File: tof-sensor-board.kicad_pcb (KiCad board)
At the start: 2 copper layers, 39 parts, among them IC1 TLV710, U1 STM32F042C6T6, U2 LTC2875, U3 VL6180X, X1 16MHz

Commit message: PCB
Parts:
- added _M2: VAL**, _mech:_M2, F.Cu at (137.1, 102.1)
- added _M2: VAL**, _mech:_M2, F.Cu at (137.1, 79.6)
- C1, C10, C11, C12, C13, C14, C15, C16, C2, C3, C4, C5, C6, C7, C8, C9, D1, D2, D3, D4, F1, IC1, R1, R10, R2, R3, R4, R5, R6, R7, R8, R9, U2, X1: moved to B.Cu
- CONN1: footprint _connectors:_Pin2mm_5z -> _connectors:_SoldarPad2mm_5; moved to B.Cu
- U3: footprint _sensors:VL6180X -> _sensors:VL6180X_EdgeMount
- moved C9 74.9 mm to (133.3, 98.1), turned to 270 degrees
- moved C11 72.7 mm to (136.8, 90.4), turned to 90 degrees
- moved C4 71.1 mm to (138.1, 90.4), turned to 90 degrees
- moved D3 67.7 mm to (143.3, 99.4), turned to 180 degrees
- moved C1 67.5 mm to (138.3, 85.7), turned to 180 degrees
- moved C10 67.0 mm to (136.5, 84.0), turned to 270 degrees
- moved C3 65.5 mm to (138.8, 93.1), turned to 180 degrees
- moved C12 65.0 mm to (135.3, 84.0), turned to 270 degrees
- moved C8 64.8 mm to (138.4, 98.0), turned to 90 degrees
- moved D4 64.7 mm to (133.0, 83.4), turned to 180 degrees
- moved R8 64.2 mm to (132.2, 86.9)
- moved C7 62.7 mm to (140.7, 83.8)
- moved C2 59.8 mm to (143.4, 95.5), turned to 180 degrees
- moved D2 59.7 mm to (143.3, 98.0), turned to 180 degrees
- moved C14 58.3 mm to (142.9, 89.4), turned to 90 degrees
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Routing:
- net GND: track 0.00 -> 111.7 mm, vias 0 -> 10
- net VCC: track 0.00 -> 46.7 mm, vias 0 -> 4
- net /2.8V: track 0.00 -> 26.7 mm, vias 0 -> 2
- net /I2C_SDA: track 0.00 -> 24.2 mm, vias 0 -> 1
- net +5V: track 0.00 -> 22.1 mm, vias 0 -> 1
- net /I2C_SCL: track 0.00 -> 21.6 mm, vias 0 -> 1
- net Net-(CONN2-Pad3): track 0.00 -> 21.4 mm, vias 0 -> 3
- net /STM32F0_SWCLK: track 0.00 -> 19.6 mm, vias 0 -> 1
- net /STM32F0_SWDIO: track 0.00 -> 19.5 mm, vias 0 -> 1
- net Net-(CONN2-Pad4): track 0.00 -> 18.7 mm, vias 0 -> 2
- net /GPIO1: track 0.00 -> 15.1 mm, vias 0 -> 1
- net /STM32F0_NRST: track 0.00 -> 13.2 mm, vias 0 -> 2
- net /GPIO0: track 0.00 -> 10.4 mm, vias 0 -> 1
- net Net-(C8-Pad1): track 0.00 -> 8.64 mm, vias 0 -> 1
- net /Error: track 0.00 -> 7.83 mm, vias 0 -> 1
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- added copper zone on F.Cu, net GND
- added copper zone on B.Cu, net VCC
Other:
- board outline added: 17 x 22.5 mm
- net class Default: clearance 0.2 -> 0.1524; trace_width 0.25 -> 0.1524
- net class Inner added: clearance 0.254, trace_width 0.204, via_dia 0.6, via_drill 0.4
- net class Power added: clearance 0.2, trace_width 0.4, via_dia 0.6, via_drill 0.4
- rule trace_clearance: 0.2 -> 0.1524
- rule trace_min: 0.2 -> 0.1524

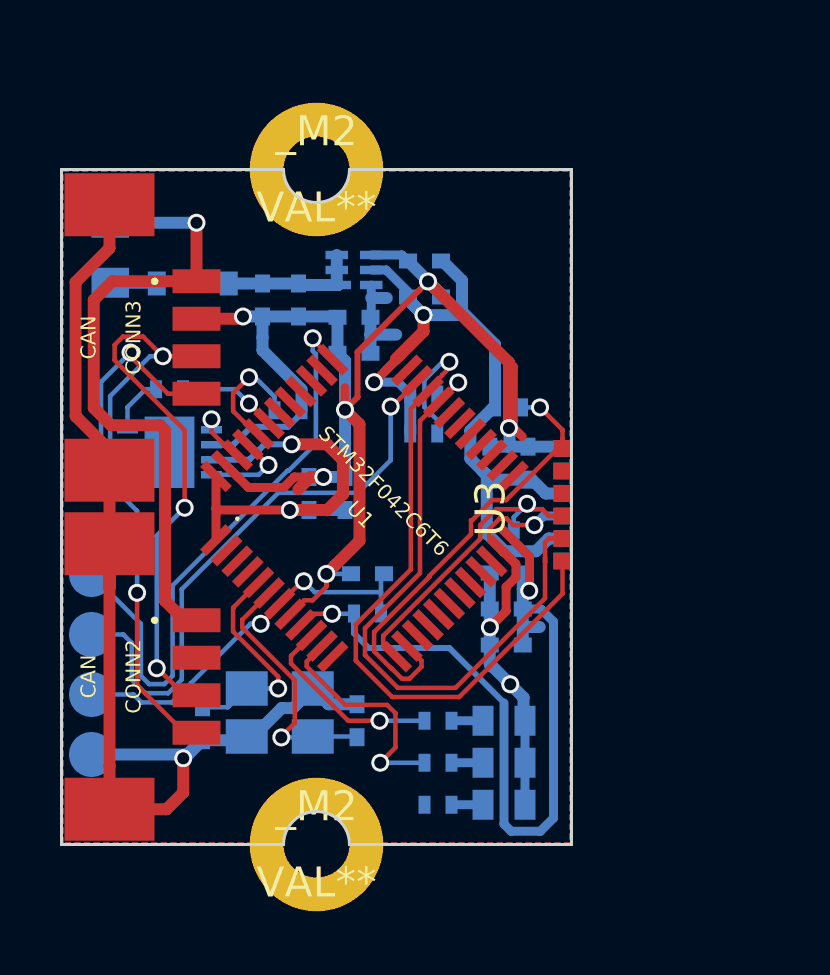
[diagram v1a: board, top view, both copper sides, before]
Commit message: Switch to VL53L0X and QFN32 STM32f302
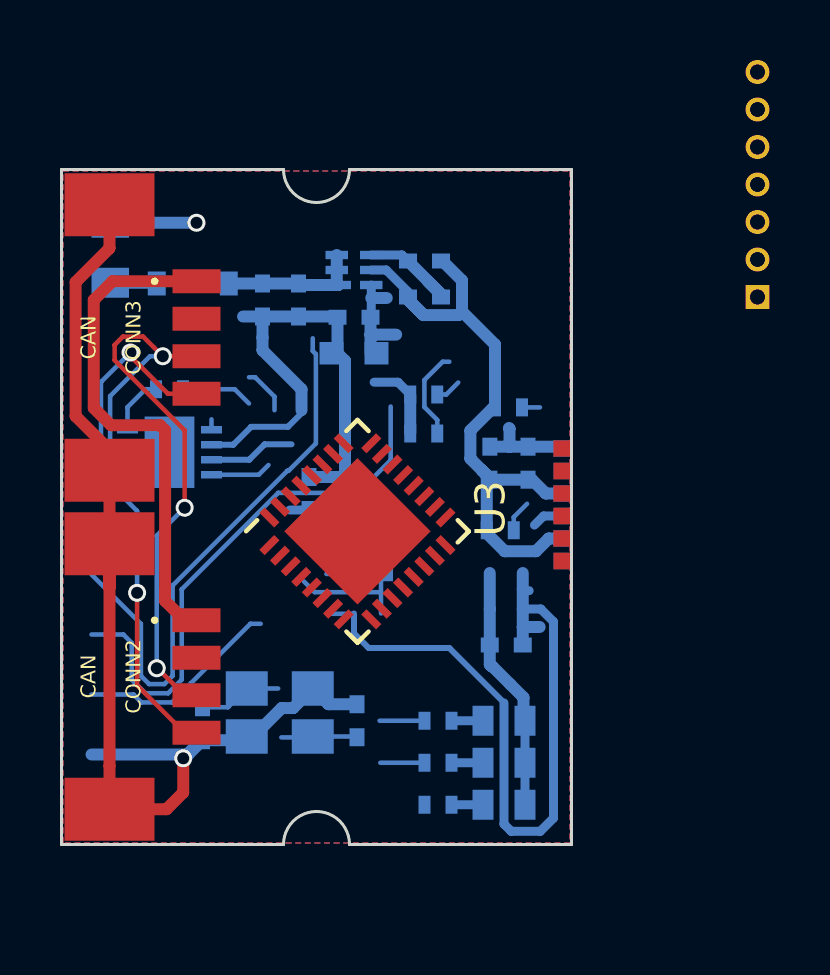
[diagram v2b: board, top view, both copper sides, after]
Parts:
- removed C4: 0.1uF, Capacitors_SMD:C_0402
- removed C5: 1uF, Capacitors_SMD:C_0402
- removed C6: 0.01uF, Capacitors_SMD:C_0402
- removed R1, R2: 100k, Resistors_SMD:R_0402
- removed _M2 (x2): VAL**, _mech:_M2
- C1: footprint Capacitors_SMD:C_0402 -> Capacitors_SMD:C_0603
- CONN1: value SWD -> SWD/DEBUG; footprint _connectors:_SoldarPad2mm_5 -> Connectors_Molex:Connector_Molex_PicoBlade_53048-0710
- U1: value STM32F042C6T6 -> STM32F302K8U6; footprint _lqfp:_LQFP48 -> Housings_DFN_QFN:QFN-32-1EP_5x5mm_Pitch0.5mm
- moved CONN1 25.9 mm to (151.8, 83.8)
- moved U1 4.72 mm to (138.5, 91.7), turned to 45 degrees
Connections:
- C2 pad 1: VCC -> GND
- C2 pad 2: GND -> VCC
- C3 pad 1: /STM32F0_NRST -> (no net)
- C7 pad 1: /2.8V -> VCC
- CONN1 pad 3: /STM32F0_NRST -> /NRST
- CONN1 pad 4: /STM32F0_SWDIO -> /SWDIO
- CONN1 pad 5: /STM32F0_SWCLK -> /SWCLK
- R3 pad 1: /2.8V -> VCC
- R4 pad 1: /2.8V -> VCC
- U1 pad 10: /Proximity -> /GPIO0
- U1 pad 11: /Error -> /GPIO1
- U1 pad 12: Net-(U1-Pad12) -> (no net)
- U1 pad 13: /GPIO0 -> (no net)
- U1 pad 14: /GPIO1 -> (no net)
- U1 pad 15: Net-(U1-Pad15) -> (no net)
- U1 pad 16: Net-(U1-Pad16) -> GND
- U1 pad 17: Net-(U1-Pad17) -> VCC
- U1 pad 18: Net-(U1-Pad18) -> (no net)
- U1 pad 19: Net-(U1-Pad19) -> /I2C_SCL
- U1 pad 2: Net-(U1-Pad2) -> Net-(C9-Pad1)
- U1 pad 20: Net-(U1-Pad20) -> /I2C_SDA
- U1 pad 21: Net-(U1-Pad21) -> /CAN_RX
- U1 pad 22: Net-(U1-Pad22) -> /CAN_TX
- U1 pad 23: GND -> /SWDIO
- U1 pad 24: VCC -> /SWCLK
- U1 pad 25: Net-(U1-Pad25) -> (no net)
- U1 pad 26: Net-(U1-Pad26) -> (no net)
- U1 pad 27: Net-(U1-Pad27) -> (no net)
- U1 pad 28: Net-(U1-Pad28) -> (no net)
- U1 pad 29: Net-(U1-Pad29) -> (no net)
- U1 pad 3: Net-(U1-Pad3) -> Net-(C8-Pad1)
- U1 pad 30: Net-(U1-Pad30) -> (no net)
- U1 pad 31: Net-(U1-Pad31) -> GND
- U1 pad 32: /I2C_SCL -> GND
- U1 pad 33: /I2C_SDA -> (no net)
- U1 pad 4: Net-(U1-Pad4) -> /NRST
- U1 pad 5: Net-(C9-Pad1) -> VCC
- U1 pad 6: Net-(C8-Pad1) -> GND
- U1 pad 7: /STM32F0_NRST -> /Proximity
- U1 pad 8: GND -> /Error
- U1 pad 9: VCC -> /CAN_SPEED
- U2 pad 5: Net-(U2-Pad5) -> (no net)
- U3 pad 11: Net-(U3-Pad11) -> (no net)
- U3 pad 2: Net-(U3-Pad2) -> (no net)
- U3 pad 3: Net-(U3-Pad3) -> (no net)
- U3 pad 7: Net-(U3-Pad7) -> (no net)
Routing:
- net /I2C_SDA: track 24.2 -> 3.04 mm, vias 1 -> 0
- net (no net): track 0.00 -> 21.0 mm
- net /I2C_SCL: track 21.6 -> 0.87 mm, vias 1 -> 0
- net /STM32F0_SWCLK: track 19.6 -> 0.00 mm, vias 1 -> 0
- net /STM32F0_SWDIO: track 19.5 -> 0.00 mm, vias 1 -> 0
- net /SWDIO: track 0.00 -> 18.6 mm
- net GND: track 111.7 -> 93.1 mm, vias 10 -> 1
- net VCC: track 46.7 -> 28.5 mm, vias 4 -> 0
- net /GPIO1: track 15.1 -> 0.60 mm, vias 1 -> 0
- net /STM32F0_NRST: track 13.2 -> 0.00 mm, vias 2 -> 0
- net /GPIO0: track 10.4 -> 1.07 mm, vias 1 -> 0
- net /2.8V: track 26.7 -> 18.3 mm, vias 2 -> 0
- net /Error: track 7.83 -> 1.47 mm, vias 1 -> 0
- net Net-(C8-Pad1): track 8.64 -> 2.55 mm, vias 1 -> 0
- net /Proximity: track 6.46 -> 1.50 mm, vias 1 -> 0
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
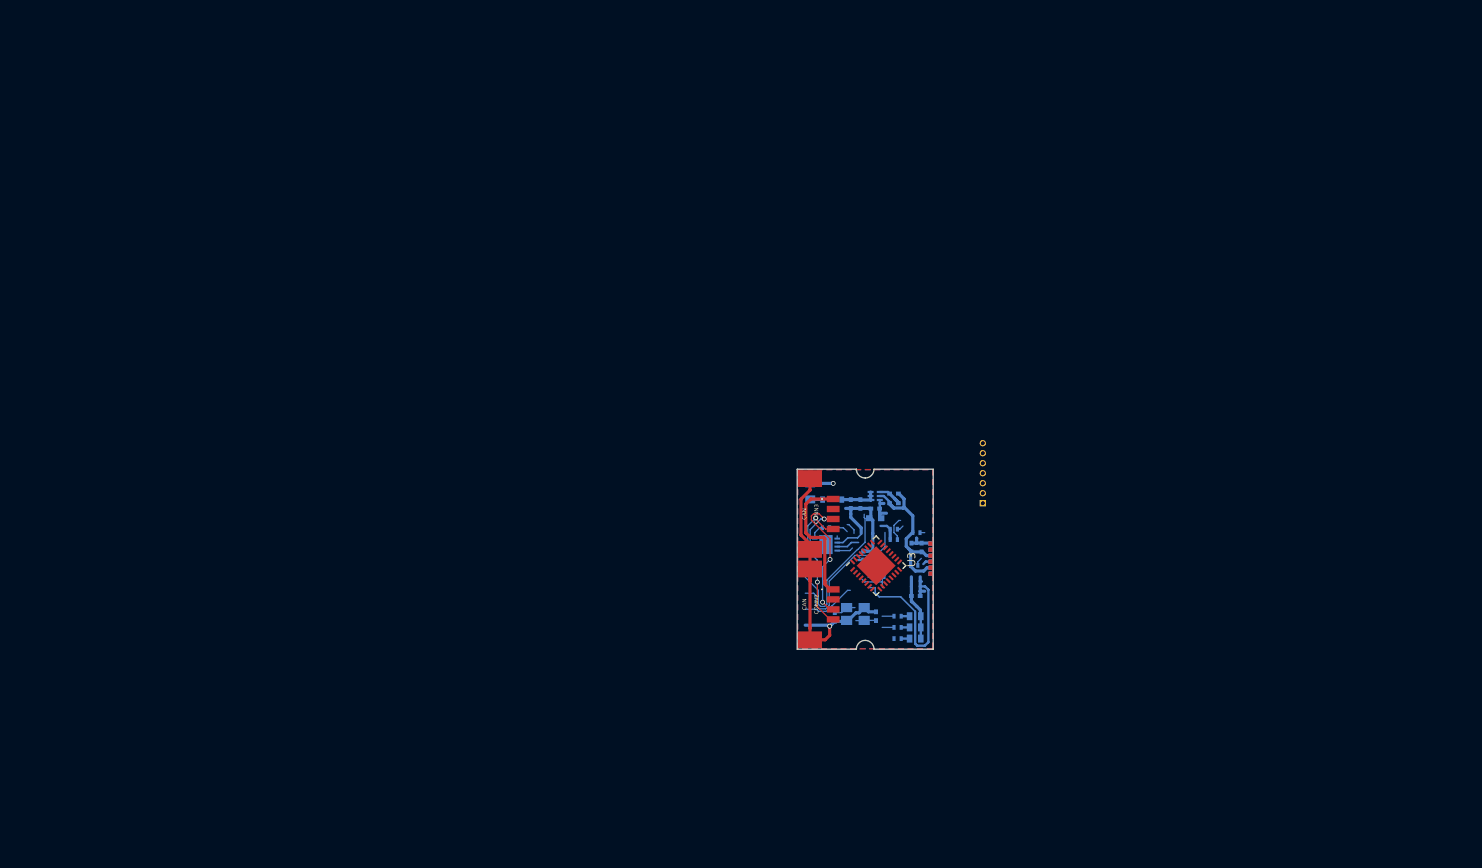
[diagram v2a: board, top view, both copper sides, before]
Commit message: Start placing footprints
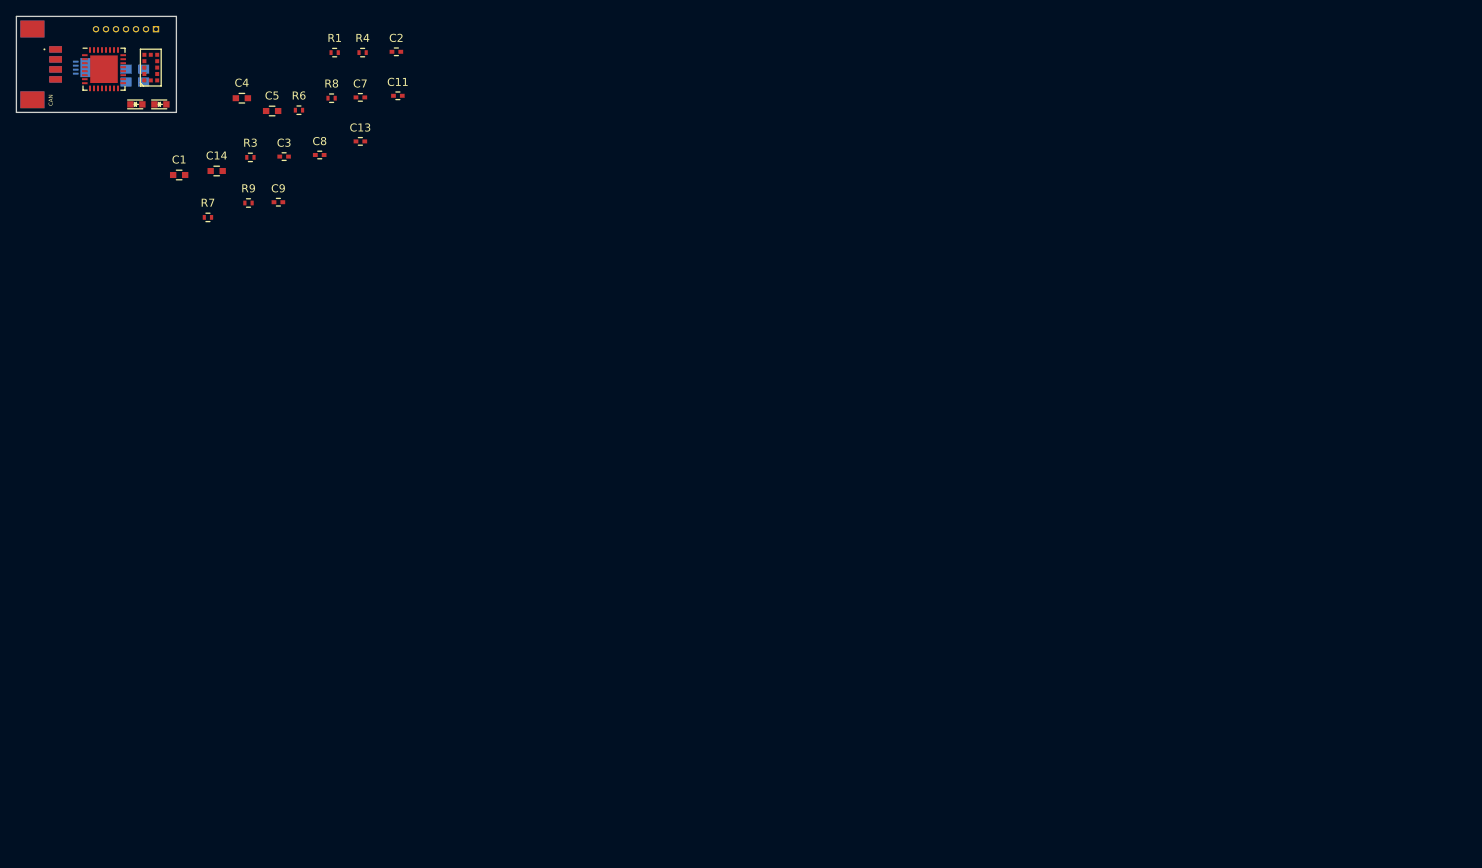
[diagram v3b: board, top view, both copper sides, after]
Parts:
- removed C10: 10uF, Capacitors_SMD:C_0402
- removed C12: 0.1uF, Capacitors_SMD:C_0402
- removed C15, C16: 4.7uF, Capacitors_SMD:C_0402
- removed D1: POWER, _std:_0603
- removed D4: SBR130S3-7, _std:_SOD-323
- removed F1: 0ZCK0050FF2E, Capacitors_SMD:C_0805
- removed IC1: TLV710, cvra:CVRA-PWSON-N6
- removed R10: 47k, Resistors_SMD:R_0402
- removed R5: 1k, Resistors_SMD:R_0402
- removed U3: VL6180X, _sensors:VL6180X_EdgeMount
- added C4: 1uF, Capacitors_SMD:C_0603, F.Cu at (59.2, 33.2)
- added C5: 22uF, Capacitors_SMD:C_0603, F.Cu at (63.0, 34.8)
- added R1: 10k, Resistors_SMD:R_0402, F.Cu at (70.8, 27.5)
- added U4: VL53L0X, _sensors:VL53L0X, F.Cu at (47.8, 29.4)
- C1, C11, C13, C2, C3, C7, C8, C9, R3, R4, R6, R7, R8: moved to F.Cu
- C14: footprint Capacitors_SMD:C_0402 -> Capacitors_SMD:C_0603; moved to F.Cu
- CONN1: footprint Connectors_Molex:Connector_Molex_PicoBlade_53048-0710 -> Connectors_Molex:Connector_Molex_PicoBlade_53047-0710
- CONN2: moved to B.Cu
- D2, D3: footprint _std:_0603 -> LEDs:LED-0603; moved to F.Cu
- R9: value 47k -> 10k; moved to F.Cu
- moved CONN1 119.1 mm to (48.5, 24.6), turned to 180 degrees
- moved CONN2 118.3 mm to (33.0, 29.0), turned to 90 degrees
- moved D2 116.5 mm to (46.0, 34.0), turned to 0 degrees
- moved D3 114.8 mm to (49.0, 34.0), turned to 0 degrees
- moved U1 114.7 mm to (42.0, 29.6), turned to 0 degrees
- moved X1 112.4 mm to (45.8, 30.4), turned to 0 degrees
- moved CONN3 112.3 mm to (33.0, 29.0)
- moved U2 110.0 mm to (39.8, 29.4)
- moved R7 100.3 mm to (54.9, 48.1), turned to 0 degrees
- moved C14 98.8 mm to (56.0, 42.3), turned to 0 degrees
- moved R6 98.0 mm to (66.3, 34.7), turned to 0 degrees
- moved C1 97.0 mm to (51.3, 42.8), turned to 0 degrees
- moved R9 94.7 mm to (60.0, 46.3)
- moved C2 94.0 mm to (78.5, 27.4), turned to 0 degrees
- moved R3 92.9 mm to (60.3, 40.6)
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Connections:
- net /GPIO0 renamed /XSHUT
- net /SWCLK renamed /STM32_SWCLK
- net /SWDIO renamed /STM32_SWDIO
- C13 pad 1: /2.8V -> VCC
- C14 pad 1: /2.8V -> VCC
- C2 pad 1: GND -> VCC
- C2 pad 2: VCC -> GND
- C3 pad 1: (no net) -> /STM32_NRST
- CONN1 pad 3: /NRST -> /STM32_NRST
- CONN1 pad 6: (no net) -> /UART2_TX
- CONN1 pad 7: (no net) -> /UART2_RX
- R9 pad 1: /2.8V -> VCC
- U1 pad 26: (no net) -> /UART2_TX
- U1 pad 27: (no net) -> /UART2_RX
- U1 pad 4: /NRST -> /STM32_NRST
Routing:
- net GND: track 93.1 -> 0.00 mm, vias 1 -> 0
- net VCC: track 28.5 -> 0.00 mm
- net Net-(CONN2-Pad3): track 21.4 -> 0.00 mm, vias 3 -> 0
- net (no net): track 21.0 -> 0.00 mm
- net +5V: track 20.2 -> 0.00 mm, vias 1 -> 0
- net Net-(CONN2-Pad4): track 18.7 -> 0.00 mm, vias 2 -> 0
- net /STM32_SWDIO: track 18.6 -> 0.00 mm
- net /2.8V: track 18.3 -> 0.00 mm
- net Net-(C10-Pad1): track 4.69 -> 0.00 mm
- net /I2C_SDA: track 3.04 -> 0.00 mm
- net Net-(U2-Pad9): track 2.85 -> 0.00 mm
- net Net-(C9-Pad1): track 2.78 -> 0.00 mm
- net Net-(C8-Pad1): track 2.55 -> 0.00 mm
- net /CAN_SPEED: track 2.40 -> 0.00 mm
- net /CAN_RX: track 2.03 -> 0.00 mm
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- removed copper zone on F.Cu, net GND
- removed copper zone on B.Cu, net VCC
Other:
- board size 17 x 22.5 mm -> 20 x 12 mm
- net class Default: clearance 0.1524 -> 0.2; trace_width 0.1524 -> 0.25
- net class Inner removed
- net class Power removed
- rule trace_clearance: 0.1524 -> 0.2
- rule trace_min: 0.1524 -> 0.15
